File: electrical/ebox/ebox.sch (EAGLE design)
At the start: 30 parts, among them IC1 MAX3221CUE, IC2 MCP170350MB, IC3 XMEGA128A1, X1 22-23-2031, X2 22-23-2031, X3 C-GRID-07-70543, X4 22-23-2021, X5 C-GRID-07-70543, X6 C-GRID-07-70543, X7 C-GRID-07-70543, X8 C-GRID-07-70543, X9 C-GRID-07-70543

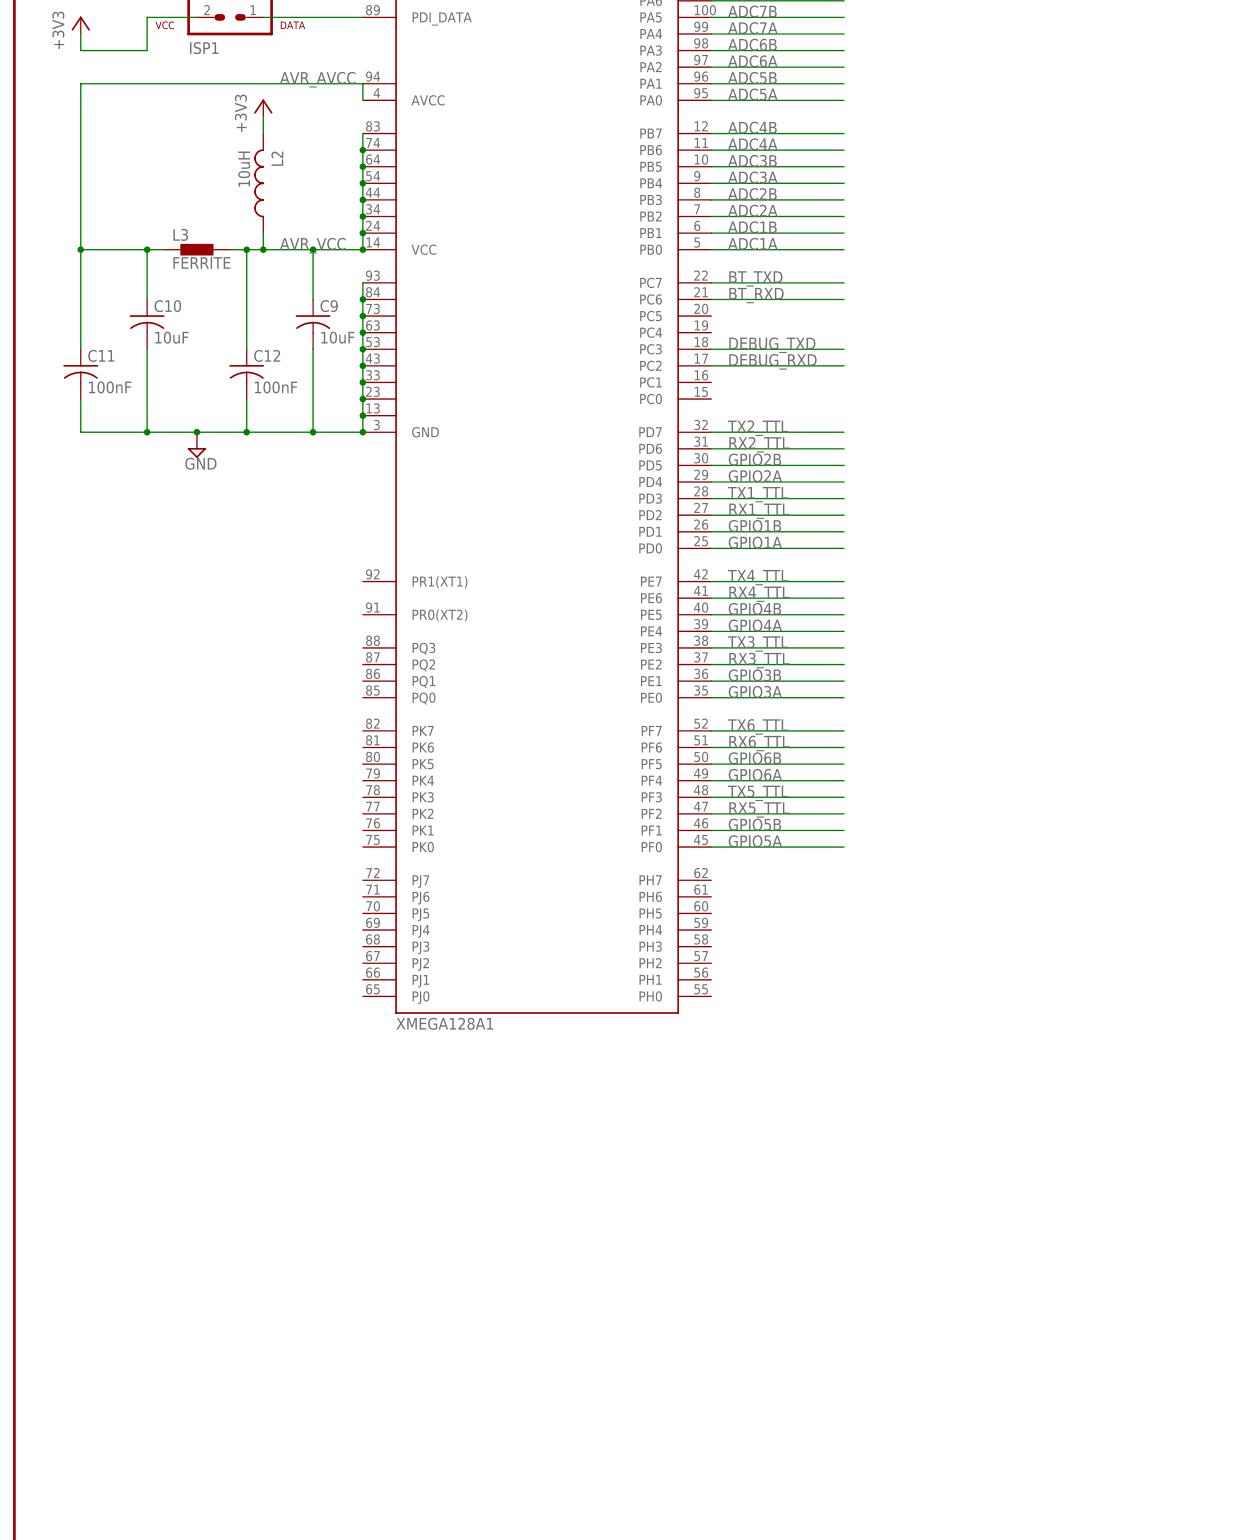
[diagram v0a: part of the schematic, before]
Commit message: Added power switch.
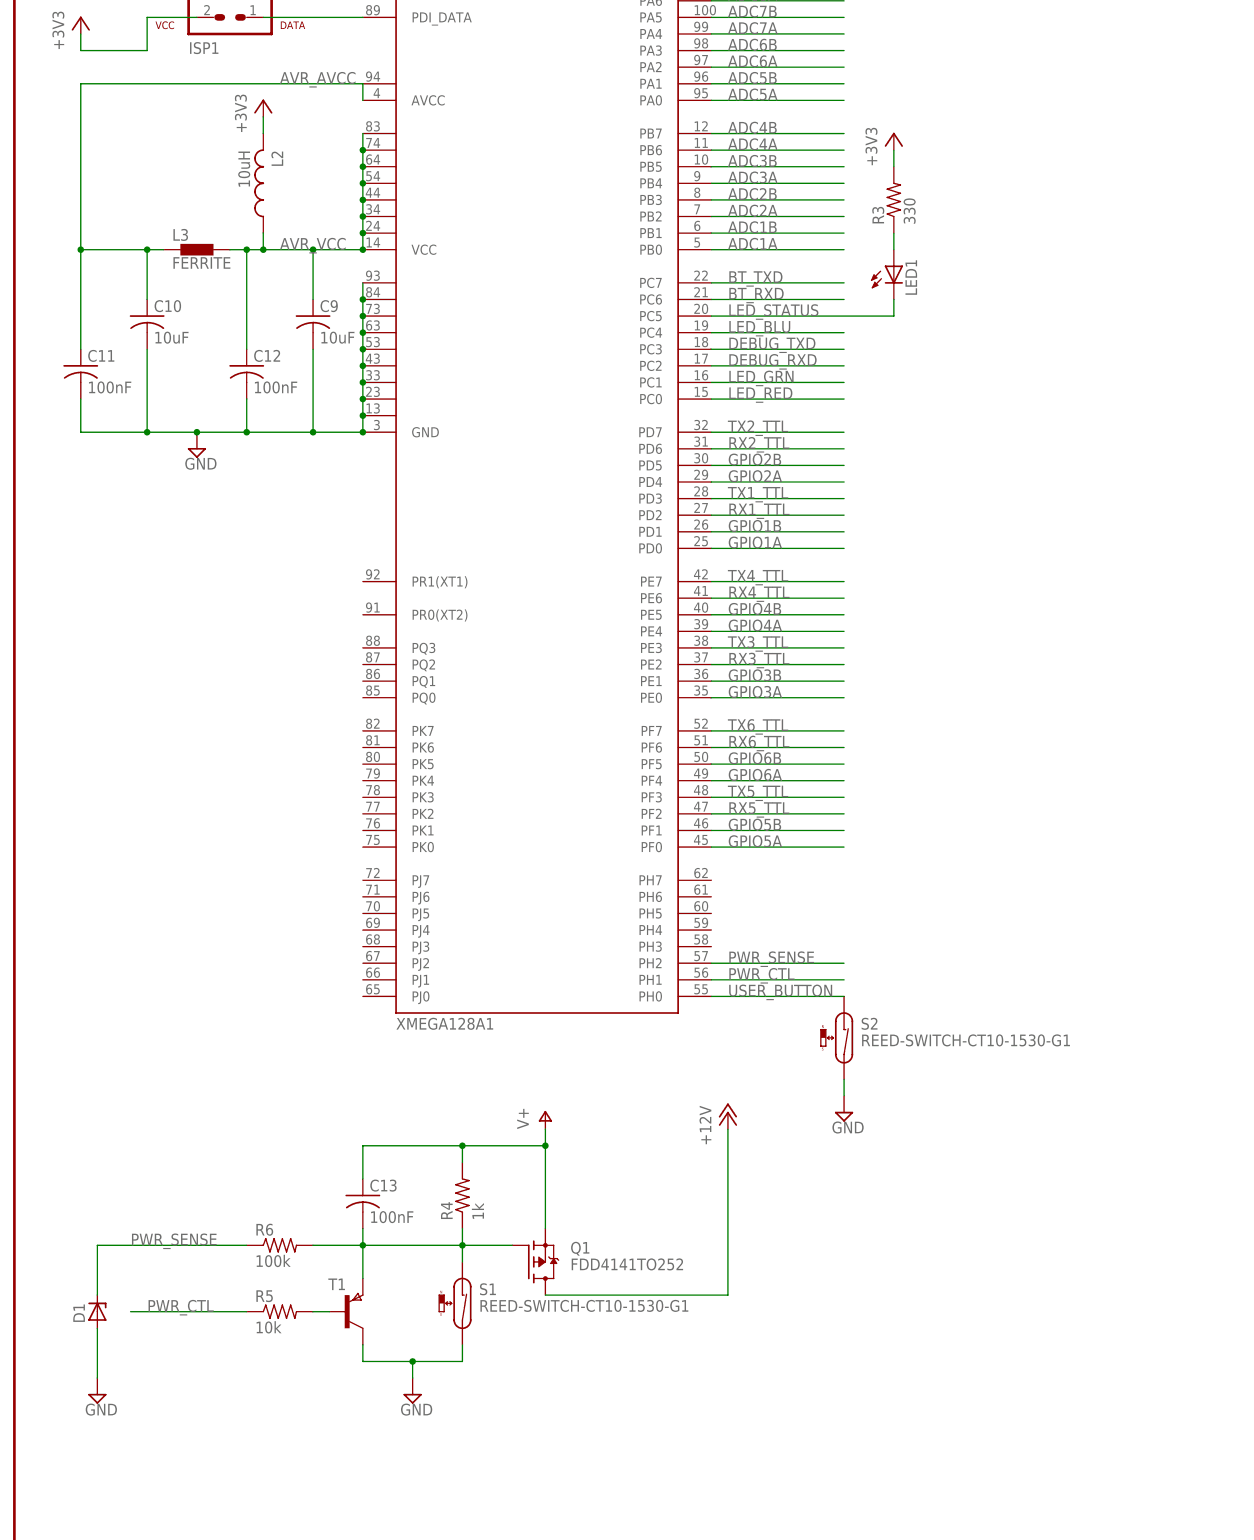
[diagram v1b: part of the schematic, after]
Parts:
- added C13: 100nF, rcl:C-USC0805
- added D1: (no value), diode:ZENER-DIODESOT23
- added LED1: (no value), led:LEDCHIPLED_1206
- added Q1: FDD4141TO252, transistor-fet:FDD4141TO252
- added R3: 330, rcl:R-US_R0805
- added R4: 1k, rcl:R-US_R0805
- added R5: 10k, rcl:R-US_R0805
- added R6: 100k, rcl:R-US_R0805
- added S1, S2: REED-SWITCH-CT10-1530-G1, switch-reed:REED-SWITCH-CT10-1530-G1
- added T1: (no value), zetex:PNPSOT23
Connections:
- new net LED_BLU: IC3.PC4
- new net LED_GRN: IC3.PC1
- new net LED_RED: IC3.PC0
- new net LED_STATUS: IC3.PC5, LED1.C
- new net N$13: C13.2, Q1.G, R4.1, R6.2, S1.1, T1.E
- new net N$6: LED1.A, R3.1
- new net N$8: R5.2, T1.B
- new net PWR_CTL: IC3.PH1, R5.1
- new net PWR_SENSE: D1.C, IC3.PH2, R6.1
- new net USER_BUTTON: IC3.PH0, S2.1
- new net V+: C13.1, Q1.S, R4.2
- net +12V: now also Q1.D
- net +3V3: now also R3.2
- net GND: now also D1.A, S1.2, S2.2, T1.C
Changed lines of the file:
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@@
 <part name="R2" library="rcl" deviceset="R-US_" device="R0805" value="10k"/>
 <part name="+3V4" library="supply1" deviceset="+3V3" device=""/>
+<part name="LED1" library="led" deviceset="LED" device="CHIPLED_1206"/>
+<part name="R3" library="rcl" deviceset="R-US_" device="R0805" value="330"/>
+<part name="+3V5" library="supply1" deviceset="+3V3" device=""/>
+<part name="S1" library="switch-reed" deviceset="REED-SWITCH-" device="CT10-1530-G1"/>
+<part name="S2" library="switch-reed" deviceset="REED-SWITCH-" device="CT10-1530-G1"/>
+<part name="SUPPLY6" library="supply2" deviceset="GND" device=""/>
+<part name="P+2" library="supply1" deviceset="+12V" device=""/>
+<part name="R4" library="rcl" deviceset="R-US_" device="R0805" value="1k"/>
+<part name="C13" library="rcl" deviceset="C-US" device="C0805" value="100nF"/>
+<part name="P+3" library="supply1" deviceset="V+" device=""/>
+<part name="SUPPLY7" library="supply2" deviceset="GND" device=""/>
+<part name="R5" library="rcl" deviceset="R-US_" device="R0805" value="10k"/>
+<part name="T1" library="zetex" deviceset="PNPSOT23" device=""/>
+<part name="R6" library="rcl" deviceset="R-US_" device="R0805" value="100k"/>
+<part name="D1" library="diode" deviceset="ZENER-DIODE" device="SOT23"/>
+<part name="SUPPLY8" library="supply2" deviceset="GND" device=""/>
+<part name="Q1" library="transistor-fet" deviceset="FDD4141" device="TO252"/>
 </parts>
 <sheets>
@@
 <instance part="R2" gate="G$1" x="48.26" y="251.46" rot="R90"/>
 <instance part="+3V4" gate="G$1" x="48.26" y="261.62"/>
+<instance part="LED1" gate="G$1" x="134.62" y="200.66"/>
+<instance part="R3" gate="G$1" x="134.62" y="210.82" rot="R90"/>
+<instance part="+3V5" gate="G$1" x="134.62" y="220.98"/>
+<instance part="S1" gate="G$1" x="68.58" y="40.64"/>
+<instance part="S2" gate="G$1" x="127" y="81.28"/>
+<instance part="SUPPLY6" gate="GND" x="127" y="71.12"/>
+<instance part="P+2" gate="1" x="109.22" y="71.12"/>
+<instance part="R4" gate="G$1" x="68.58" y="58.42" rot="R90"/>
+<instance part="C13" gate="G$1" x="53.34" y="58.42"/>
+<instance part="P+3" gate="1" x="81.28" y="71.12"/>
+<instance part="SUPPLY7" gate="GND" x="60.96" y="27.94"/>
+<instance part="R5" gate="G$1" x="40.64" y="40.64"/>
+<instance part="T1" gate="A" x="50.8" y="40.64" smashed="yes">
+<attribute name="NAME" x="50.8" y="45.72" size="1.778" layer="95" rot="R180"/>
+<attribute name="VALUE" x="40.64" y="45.72" size="1.778" layer="96"/>
+</instance>
+<instance part="R6" gate="G$1" x="40.64" y="50.8"/>
+<instance part="D1" gate="G$1" x="12.7" y="40.64" rot="R90"/>
+<instance part="SUPPLY8" gate="GND" x="12.7" y="27.94"/>
+<instance part="Q1" gate="G$1" x="78.74" y="48.26" smashed="yes">
+<attribute name="VALUE" x="85.09" y="46.99" size="1.778" layer="96"/>
+<attribute name="NAME" x="85.09" y="49.53" size="1.778" layer="95"/>
+</instance>
 </instances>
 <busses>
@@
 <pinref part="SUPPLY5" gate="GND" pin="GND"/>
 </segment>
+<segment>
+<pinref part="S2" gate="G$1" pin="2"/>
+<pinref part="SUPPLY6" gate="GND" pin="GND"/>
+<wire x1="127" y1="73.66" x2="127" y2="76.2" width="0.1524" layer="91"/>
+</segment>
+<segment>
+<wire x1="53.34" y1="35.56" x2="53.34" y2="33.02" width="0.1524" layer="91"/>
+<wire x1="53.34" y1="33.02" x2="60.96" y2="33.02" width="0.1524" layer="91"/>
+<pinref part="SUPPLY7" gate="GND" pin="GND"/>
+<wire x1="60.96" y1="33.02" x2="60.96" y2="30.48" width="0.1524" layer="91"/>
+<pinref part="S1" gate="G$1" pin="2"/>
+<wire x1="68.58" y1="35.56" x2="68.58" y2="33.02" width="0.1524" layer="91"/>
+<wire x1="68.58" y1="33.02" x2="60.96" y2="33.02" width="0.1524" layer="91"/>
+<junction x="60.96" y="33.02"/>
+<pinref part="T1" gate="A" pin="C"/>
+</segment>
+<segment>
+<pinref part="D1" gate="G$1" pin="A"/>
+<pinref part="SUPPLY8" gate="GND" pin="GND"/>
+<wire x1="12.7" y1="38.1" x2="12.7" y2="30.48" width="0.1524" layer="91"/>
+</segment>
 </net>
 <net name="S1_12V" class="0">
@@
 <pinref part="+3V4" gate="G$1" pin="+3V3"/>
 </segment>
+<segment>
+<pinref part="+3V5" gate="G$1" pin="+3V3"/>
+<pinref part="R3" gate="G$1" pin="2"/>
+<wire x1="134.62" y1="218.44" x2="134.62" y2="215.9" width="0.1524" layer="91"/>
+</segment>
 </net>
 <net name="+12V" class="0">
@@
 <pinref part="P+1" gate="1" pin="+12V"/>
 <junction x="241.3" y="175.26"/>
+</segment>
+<segment>
+<wire x1="81.28" y1="43.18" x2="109.22" y2="43.18" width="0.1524" layer="91"/>
+<pinref part="P+2" gate="1" pin="+12V"/>
+<wire x1="109.22" y1="43.18" x2="109.22" y2="68.58" width="0.1524" layer="91"/>
+<pinref part="Q1" gate="G$1" pin="D"/>
 </segment>
 </net>
@@
 </segment>
 </net>
+<net name="LED_STATUS" class="0">
+<segment>
+<pinref part="IC3" gate="G$1" pin="PC5"/>
+<wire x1="106.68" y1="193.04" x2="134.62" y2="193.04" width="0.1524" layer="91"/>
+<label x="109.22" y="193.04" size="1.778" layer="95"/>
+<pinref part="LED1" gate="G$1" pin="C"/>
+<wire x1="134.62" y1="193.04" x2="134.62" y2="195.58" width="0.1524" layer="91"/>
+</segment>
+</net>
+<net name="LED_BLU" class="0">
+<segment>
+<pinref part="IC3" gate="G$1" pin="PC4"/>
+<wire x1="106.68" y1="190.5" x2="127" y2="190.5" width="0.1524" layer="91"/>
+<label x="109.22" y="190.5" size="1.778" layer="95"/>
+</segment>
+</net>
+<net name="LED_RED" class="0">
+<segment>
+<pinref part="IC3" gate="G$1" pin="PC0"/>
+<wire x1="106.68" y1="180.34" x2="127" y2="180.34" width="0.1524" layer="91"/>
+<label x="109.22" y="180.34" size="1.778" layer="95"/>
+</segment>
+</net>
+<net name="LED_GRN" class="0">
+<segment>
+<pinref part="IC3" gate="G$1" pin="PC1"/>
+<wire x1="106.68" y1="182.88" x2="127" y2="182.88" width="0.1524" layer="91"/>
+<label x="109.22" y="182.88" size="1.778" layer="95"/>
+</segment>
+</net>
+<net name="N$6" class="0">
+<segment>
+<pinref part="LED1" gate="G$1" pin="A"/>
+<wire x1="134.62" y1="203.2" x2="134.62" y2="205.74" width="0.1524" layer="91"/>
+<pinref part="R3" gate="G$1" pin="1"/>
+</segment>
+</net>
+<net name="USER_BUTTON" class="0">
+<segment>
+<pinref part="IC3" gate="G$1" pin="PH0"/>
+<pinref part="S2" gate="G$1" pin="1"/>
+<wire x1="106.68" y1="88.9" x2="127" y2="88.9" width="0.1524" layer="91"/>
+<label x="109.22" y="88.9" size="1.778" layer="95"/>
+</segment>
+</net>
+<net name="V+" class="0">
+<segment>
+<pinref part="P+3" gate="1" pin="V+"/>
+<wire x1="81.28" y1="68.58" x2="81.28" y2="66.04" width="0.1524" layer="91"/>
+<pinref part="C13" gate="G$1" pin="1"/>
+<wire x1="81.28" y1="66.04" x2="81.28" y2="53.34" width="0.1524" layer="91"/>
+<wire x1="53.34" y1="66.04" x2="53.34" y2="60.96" width="0.1524" layer="91"/>
+<wire x1="53.34" y1="66.04" x2="68.58" y2="66.04" width="0.1524" layer="91"/>
+<pinref part="R4" gate="G$1" pin="2"/>
+<wire x1="68.58" y1="63.5" x2="68.58" y2="66.04" width="0.1524" layer="91"/>
+<junction x="68.58" y="66.04"/>
+<wire x1="68.58" y1="66.04" x2="81.28" y2="66.04" width="0.1524" layer="91"/>
+<junction x="81.28" y="66.04"/>
+<pinref part="Q1" gate="G$1" pin="S"/>
+</segment>
+</net>
+<net name="N$13" class="0">
+<segment>
+<pinref part="C13" gate="G$1" pin="2"/>
+<wire x1="53.34" y1="53.34" x2="53.34" y2="50.8" width="0.1524" layer="91"/>
+<wire x1="53.34" y1="50.8" x2="68.58" y2="50.8" width="0.1524" layer="91"/>
+<pinref part="R4" gate="G$1" pin="1"/>
+<wire x1="68.58" y1="50.8" x2="68.58" y2="53.34" width="0.1524" layer="91"/>
+<wire x1="68.58" y1="50.8" x2="76.2" y2="50.8" width="0.1524" layer="91"/>
+<junction x="68.58" y="50.8"/>
+<wire x1="53.34" y1="50.8" x2="53.34" y2="45.72" width="0.1524" layer="91"/>
+<pinref part="S1" gate="G$1" pin="1"/>
+<wire x1="68.58" y1="48.26" x2="68.58" y2="50.8" width="0.1524" layer="91"/>
+<junction x="53.34" y="50.8"/>
+<pinref part="T1" gate="A" pin="E"/>
+<pinref part="R6" gate="G$1" pin="2"/>
+<wire x1="45.72" y1="50.8" x2="53.34" y2="50.8" width="0.1524" layer="91"/>
+<pinref part="Q1" gate="G$1" pin="G"/>
+</segment>
+</net>
+<net name="N$8" class="0">
+<segment>
+<pinref part="R5" gate="G$1" pin="2"/>
+<pinref part="T1" gate="A" pin="B"/>
+<wire x1="45.72" y1="40.64" x2="48.26" y2="40.64" width="0.1524" layer="91"/>
+</segment>
+</net>
+<net name="PWR_CTL" class="0">
+<segment>
+<pinref part="R5" gate="G$1" pin="1"/>
+<wire x1="35.56" y1="40.64" x2="17.78" y2="40.64" width="0.1524" layer="91"/>
+<label x="20.32" y="40.64" size="1.778" layer="95"/>
+</segment>
+<segment>
+<pinref part="IC3" gate="G$1" pin="PH1"/>
+<wire x1="106.68" y1="91.44" x2="127" y2="91.44" width="0.1524" layer="91"/>
+<label x="109.22" y="91.44" size="1.778" layer="95"/>
+</segment>
+</net>
+<net name="PWR_SENSE" class="0">
+<segment>
+<pinref part="R6" gate="G$1" pin="1"/>
+<label x="17.78" y="50.8" size="1.778" layer="95"/>
+<pinref part="D1" gate="G$1" pin="C"/>
+<wire x1="12.7" y1="43.18" x2="12.7" y2="50.8" width="0.1524" layer="91"/>
+<wire x1="12.7" y1="50.8" x2="35.56" y2="50.8" width="0.1524" layer="91"/>
+</segment>
+<segment>
+<pinref part="IC3" gate="G$1" pin="PH2"/>
+<wire x1="106.68" y1="93.98" x2="127" y2="93.98" width="0.1524" layer="91"/>
+<label x="109.22" y="93.98" size="1.778" layer="95"/>
+</segment>
+</net>

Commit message: Updated ebox a bit.
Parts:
- added PTC1, PTC2: 50mA, rcl:R-US_R1206
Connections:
- net S1_AN_A: now also PTC1.2
- net S1_AN_B: now also PTC2.2
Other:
- note added: "Use the: LT1161 for +12V"
- note removed: "Remember to use magnetic buttons"
- note removed: "Use the: 50mA PTC on all signal lines (R1206)"
- note removed: "Use the: Zetex FET for +12V"
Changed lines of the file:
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@@
 <part name="SUPPLY8" library="supply2" deviceset="GND" device=""/>
 <part name="Q1" library="transistor-fet" deviceset="FDD4141" device="TO252"/>
+<part name="PTC1" library="rcl" deviceset="R-US_" device="R1206" value="50mA"/>
+<part name="PTC2" library="rcl" deviceset="R-US_" device="R1206" value="50mA"/>
 </parts>
 <sheets>
@@
 <text x="236.22" y="48.26" size="1.778" layer="94">Use the: SN74LVC1T45?</text>
 <text x="236.22" y="40.64" size="1.778" layer="94">Use the: SOT23 Dual Zener (5.1V, UC3 is 5V tolerant)</text>
-<text x="236.22" y="38.1" size="1.778" layer="94">Use the: 50mA PTC on all signal lines (R1206)</text>
-<text x="236.22" y="58.42" size="1.778" layer="94">Use the: Zetex FET for +12V</text>
+<text x="236.22" y="58.42" size="1.778" layer="94">Use the: LT1161 for +12V</text>
 <text x="236.22" y="55.88" size="1.778" layer="94">Use the: 1.5A PTC on +12V (R1812)</text>
 <text x="236.22" y="50.8" size="1.778" layer="94">Use Mike's LED Strips?</text>
-<text x="236.22" y="33.02" size="1.778" layer="94">Remember to use magnetic buttons</text>
 </plain>
 <instances>
@@
 <attribute name="NAME" x="85.09" y="49.53" size="1.778" layer="95"/>
 </instance>
+<instance part="PTC1" gate="G$1" x="261.62" y="152.4"/>
+<instance part="PTC2" gate="G$1" x="261.62" y="142.24"/>
 </instances>
 <busses>
@@
 <label x="353.06" y="193.04" size="1.778" layer="95"/>
 </segment>
+<segment>
+<pinref part="PTC1" gate="G$1" pin="2"/>
+<wire x1="266.7" y1="152.4" x2="281.94" y2="152.4" width="0.1524" layer="91"/>
+<label x="269.24" y="152.4" size="1.778" layer="95"/>
+</segment>
 </net>
 <net name="S1_AN_B" class="0">
@@
 <label x="353.06" y="190.5" size="1.778" layer="95"/>
 </segment>
-</net>
+<segment>
+<pinref part="PTC2" gate="G$1" pin="2"/>
+<wire x1="266.7" y1="142.24" x2="281.94" y2="142.24" width="0.1524" layer="91"/>
+<label x="269.24" y="142.24" size="1.778" layer="95"/>
+</segment>
+</net>

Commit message: Added sparkfun library.
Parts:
- added C14: 0.1uF, rcl:C-USC0805
- added D2: GSOT05C, zetex:D_2CSOT23
- added LED2: (no value), led:LEDCHIPLED_1206
- added R7: 330, rcl:R-US_R0805
- added U$1: BLUETOOTH-RN41", SparkFun-RF:BLUETOOTH-RN41"
- C11, C12, C13: value 100nF -> 0.1uF
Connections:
- net GPIO5A renamed MOT_SERVO1
- net GPIO5B renamed MOT_SERVO2
- net S1_AN_A renamed S1_GPIO_A
- net S1_AN_B renamed S1_GPIO_B
- removed net ADC1A: IC3.PB0
- removed net ADC1B: IC3.PB1
- removed net ADC2A: IC3.PB2
- removed net ADC2B: IC3.PB3
- removed net ADC3A: IC3.PB4
- removed net ADC3B: IC3.PB5
- removed net ADC4A: IC3.PB6
- removed net ADC4B: IC3.PB7
- removed net ADC5A: IC3.PA0
- removed net ADC5B: IC3.PA1
- removed net ADC6A: IC3.PA2
- removed net ADC6B: IC3.PA3
- removed net ADC7A: IC3.PA4
- removed net ADC7B: IC3.PA5
- removed net ADC8A: IC3.PA6
- removed net ADC8B: IC3.PA7
- removed net GPIO6A: IC3.PF4
- removed net GPIO6B: IC3.PF5
- removed net RX5_TTL: IC3.PF2
- removed net RX6_TTL: IC3.PF6
- removed net TX5_TTL: IC3.PF3
- removed net TX6_TTL: IC3.PF7
- new net BT_RESET: IC3.PJ0, U$1.RESET
- new net BT_STATUS: IC3.PJ1, U$1.PIO2
- new net LED_STATUS1: LED2.C, U$1.PIO5
- new net N$9: LED2.A, R7.1
- net +3V3: now also C14.1, R7.2, U$1.VDD
- net BT_RXD: now also U$1.UARTTX
- net BT_TXD: now also U$1.UARTRX
- net GND: now also C14.2, D2.A, U$1.GND, U$1.GND1, U$1.GND2, U$1.GND3, U$1.GND4, U$1.GND5
- net GPIO1A: now also D2.C1, IC3.PB0, PTC1.1
- net GPIO1B: now also D2.C2, IC3.PB1, IC3.PB3, PTC2.1
- net GPIO2A: now also IC3.PB2
- net GPIO3A: now also IC3.PB4
- net GPIO3B: now also IC3.PB5
- net GPIO4A: now also IC3.PB6
- net GPIO4B: now also IC3.PB7
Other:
- note added: "Add BLMC connections."
- note added: "Add charging circuit"
- note added: "Add main power regulator"
- note removed: "Use the: SOT23 Dual Zener (5.1V, UC3 is 5V tolerant)"
- moved on the sheet: C13, D1, PTC1, PTC2, Q1, R4, R5, R6, S1, T1
